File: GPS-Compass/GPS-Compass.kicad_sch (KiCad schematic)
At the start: 117 parts, among them IC1 TPS565242DRLR, J2 FFC2B28-12-G, J3 Motor_conn, J4 USB_TypeC, J5 FFC2B28-12-G, J7 01x10, M1 Stepper_Motor_bipolar, Q1 Q_PMOS, Q2 Q_PMOS, SW8 RESET, SW9 BOOT, U1 DRV8834RGER, U2 AP62300Z6, U3 USBLC6-2SC6, U4 ESP32-S3-WROOM-1, U5 BQ25887

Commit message: layout updates
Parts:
- BZ1: footprint gps-compass_brd:CEM-1203_Buzzer -> inset:AST0827MW-03BTRQ_MAL
- J2: renamed from J3; footprint (none) -> Connector_JST:JST_XH_B4B-XH-A_1x04_P2.50mm_Vertical
- renumbered C2 to C1, C13 to C10, C14 to C11, C15 to C12, C16 to C13, C17 to C14, C18 to C15, C19 to C16, C20 to C17, C21 to C18, C22 to C19, C3 to C2, C23 to C20, C24 to C21, C25 to C22, C26 to C23, C27 to C24, C28 to C25, C29 to C26, C5 to C3, C6 to C4, C7 to C5, C8 to C6, C10 to C7, C11 to C8, C12 to C9, J2 to J1, J5 to J3, J7 to J4, J4 to J5, R18 to R10, R19 to R11, R20 to R12, R21 to R13, R22 to R14, R23 to R15, R24 to R16, R25 to R17, R26 to R18, R27 to R19, R28 to R20, R29 to R21, R30 to R22, R31 to R23, R32 to R24, R33 to R25, R34 to R26, R35 to R27, R36 to R28, R37 to R29, R6 to R3, R38 to R30, R39 to R31, R40 to R32, R41 to R33, R42 to R34, R43 to R35, R44 to R36, R45 to R37, R7 to R4, R9 to R5, R12 to R6, R13 to R7, R14 to R8, R15 to R9, SW8 to SW1, SW9 to SW2
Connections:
- net DN_IN: no longer J5.A6 (DP1)
- net DP_IN: now also J5.A6 (DP1)
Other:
- moved on the sheet: J1, J3, M1

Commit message: layout updates
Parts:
- SW1: footprint Connector_Wire:SolderWire-0.1sqmm_1x02_P3.6mm_D0.4mm_OD1mm_Relief -> gps-compass_brd:SW_SPST_EVQPE1
- SW2: footprint Button_Switch_SMD:SW_SPST_B3U-1000P -> gps-compass_brd:SW_SPST_EVQPE1
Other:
- moved on the sheet: SW1

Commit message: routing
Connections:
- net +3V3: now also J3.11; no longer J3.2
- net +5V: now also J1.1, J1.2, J1.3; no longer J1.10, J1.11, J1.12
- net +8V: now also J3.3; no longer J3.10
- net CLK: now also J1.6; no longer J1.7
- net CRD_RST: now also J3.6; no longer J3.7
- net EN: now also J3.4; no longer J3.9
- net EXT0: now also J3.10; no longer J3.3
- net EXT1: now also J3.8; no longer J3.5
- net EXT2: now also J3.5; no longer J3.8
- net GND: now also J1.5, J1.7, J1.9, J3.9; no longer J1.4, J1.6, J1.8, J3.4
- net GNSS_RST: now also J3.2; no longer J3.11
- net LED_EXT0: now also J3.7; no longer J3.6
- net LED_EXT1: now also J3.12; no longer J3.1
- net MOSI: now also J1.4; no longer J1.9
- net MSW_ON: now also J3.1; no longer J3.12
- net ~{CS}: now also J1.8; no longer J1.5

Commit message: will be remaking the charger probably
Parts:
- removed JP5: Jumper, Jumper:SolderJumper-2_P1.3mm_Open_RoundedPad1.0x1.5mm, symbol Jumper:Jumper_2_Small_Open
- J2: footprint Connector_JST:JST_XH_B4B-XH-A_1x04_P2.50mm_Vertical -> Connector_JST:JST_XH_S4B-XH-SM4-TB_1x04-1MP_P2.50mm_Horizontal
- R36: value 0R -> 220R
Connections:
- net USB_VBUS: now also Q2.1 (G), R18.1
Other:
- note added: "1. FUEL GAUGE 2. LiPo/Li-Ion 3. 4. 5. 6. 7."
- note added: "https://cz.mouser.com/ProductDetail/Texas-Instruments/BQ25895MRTWR?qs=uNh9J9Y3wTe%2F%252BmcQbu7CLA%3D%3D"
- note removed: "1. BUTTONS? 2. FINISH SCHEMATIC 3. BOARD LAYOUT 4. 5. CONNECTORS 6. 7."
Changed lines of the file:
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@@
 	(rectangle
 		(start 300.99 163.195)
-		(end 427.355 281.305)
+		(end 427.355 281.94)
 		(stroke
 			(width 1)
@@
 		)
 	)
-	(text "1. BUTTONS?\n2. FINISH SCHEMATIC\n3. BOARD LAYOUT\n4. \n5. CONNECTORS\n6. \n7."
+	(text "1. FUEL GAUGE\n2. LiPo/Li-Ion\n3. \n4. \n5. \n6. \n7."
 		(exclude_from_sim no)
 		(at 19.685 307.975 0)
@@
 		)
 	)
+	(text "https://cz.mouser.com/ProductDetail/Texas-Instruments/BQ25895MRTWR?qs=uNh9J9Y3wTe%2F%252BmcQbu7CLA%3D%3D"
+		(exclude_from_sim no)
+		(at 361.95 144.145 0)
+		(effects
+			(font
+				(size 1.27 1.27)
+			)
+		)
+	)
 	(text "probs not meant to be connected to the MCU"
 		(exclude_from_sim no)
@@
 	(wire
 		(pts
-			(xy 323.85 59.69) (xy 325.12 59.69)
-		)
-		(stroke
-			(width 0)
-			(type default)
-		)
-	)
-	(wire
-		(pts
 			(xy 355.6 101.6) (xy 358.14 101.6)
 		)
@@
 	(wire
 		(pts
-			(xy 313.69 59.69) (xy 318.77 59.69)
+			(xy 318.77 59.69) (xy 325.12 59.69)
 		)
 		(stroke
@@
 	(wire
 		(pts
-			(xy 313.69 59.69) (xy 313.69 58.42)
+			(xy 318.77 59.69) (xy 318.77 58.42)
 		)
 		(stroke
@@
 	)
 	(image
-		(at -70.104 42.926)
+		(at -61.849 206.121)
 		(scale 0.414908)
 		(data "iVBORw0KGgoAAAANSUhEUgAAAh4AAAH+CAIAAABcDZACAAAAA3NCSVQICAjb4U/gAAAACXBIWXMA"
@@
 	)
 	(image
-		(at -72.771 111.76)
+		(at 494.919 116.84)
 		(scale 0.27793)
 		(data "iVBORw0KGgoAAAANSUhEUgAAAsgAAAJLCAIAAAB17fdXAAAAA3NCSVQICAjb4U/gAAAACXBIWXMA"
@@
 	)
 	(symbol
-		(lib_id "Jumper:Jumper_2_Small_Open")
-		(at 321.31 59.69 0)
-		(unit 1)
-		(exclude_from_sim no)
-		(in_bom no)
-		(on_board yes)
-		(dnp no)
-		(property "Reference" "JP5"
-			(at 321.31 55.245 0)
-			(effects
-				(font
-					(size 1 1)
-				)
-			)
-		)
-		(property "Value" "Jumper"
-			(at 321.31 57.15 0)
-			(effects
-				(font
-					(size 1 1)
-				)
-			)
-		)
-		(property "Footprint" "Jumper:SolderJumper-2_P1.3mm_Open_RoundedPad1.0x1.5mm"
-			(at 321.31 59.69 0)
-			(effects
-				(font
-					(size 1.27 1.27)
-				)
-				(hide yes)
-			)
-		)
-		(property "Datasheet" "~"
-			(at 321.31 59.69 0)
-			(effects
-				(font
-					(size 1.27 1.27)
-				)
-				(hide yes)
-			)
-		)
-		(property "Description" "Jumper, 2-pole, small symbol, open"
-			(at 321.31 59.69 0)
-			(effects
-				(font
-					(size 1.27 1.27)
-				)
-				(hide yes)
-			)
-		)
-		(pin "1"
-		)
-		(pin "2"
-		)
-		(instances
-			(project "GPS-Compass"
-				(path "/944f168e-b689-4be9-b5f1-4ef8c625b176"
-					(reference "JP5")
-					(unit 1)
-				)
-			)
-		)
-	)
-	(symbol
 		(lib_id "power:+3V3")
 		(at 55.88 198.12 90)
@@
 			)
 		)
-		(property "Footprint" "Connector_JST:JST_XH_B4B-XH-A_1x04_P2.50mm_Vertical"
+		(property "Footprint" "Connector_JST:JST_XH_S4B-XH-SM4-TB_1x04-1MP_P2.50mm_Horizontal"
 			(at 115.57 195.58 0)
 			(effects
@@
 	(symbol
 		(lib_id "power:+5V")
-		(at 313.69 58.42 0)
+		(at 318.77 58.42 0)
 		(unit 1)
 		(exclude_from_sim no)
@@
 		(dnp no)
 		(property "Reference" "#PWR066"
-			(at 313.69 62.23 0)
+			(at 318.77 62.23 0)
 			(effects
 				(font
@@
 		)
 		(property "Value" "USB_VBUS"
-			(at 313.69 54.61 0)
+			(at 318.77 54.61 0)
 			(effects
 				(font
@@
 		)
 		(property "Footprint" ""
-			(at 313.69 58.42 0)
+			(at 318.77 58.42 0)
 			(effects
 				(font
@@
 		)
 		(property "Datasheet" ""
-			(at 313.69 58.42 0)
+			(at 318.77 58.42 0)
 			(effects
 				(font
@@
 		)
 		(property "Description" "Power symbol creates a global label with name \"+5V\""
-			(at 313.69 58.42 0)
+			(at 318.77 58.42 0)
 			(effects
 				(font
@@
 			)
 		)
-		(property "Value" "0R"
+		(property "Value" "220R"
 			(at 400.685 227.33 0)
 			(effects

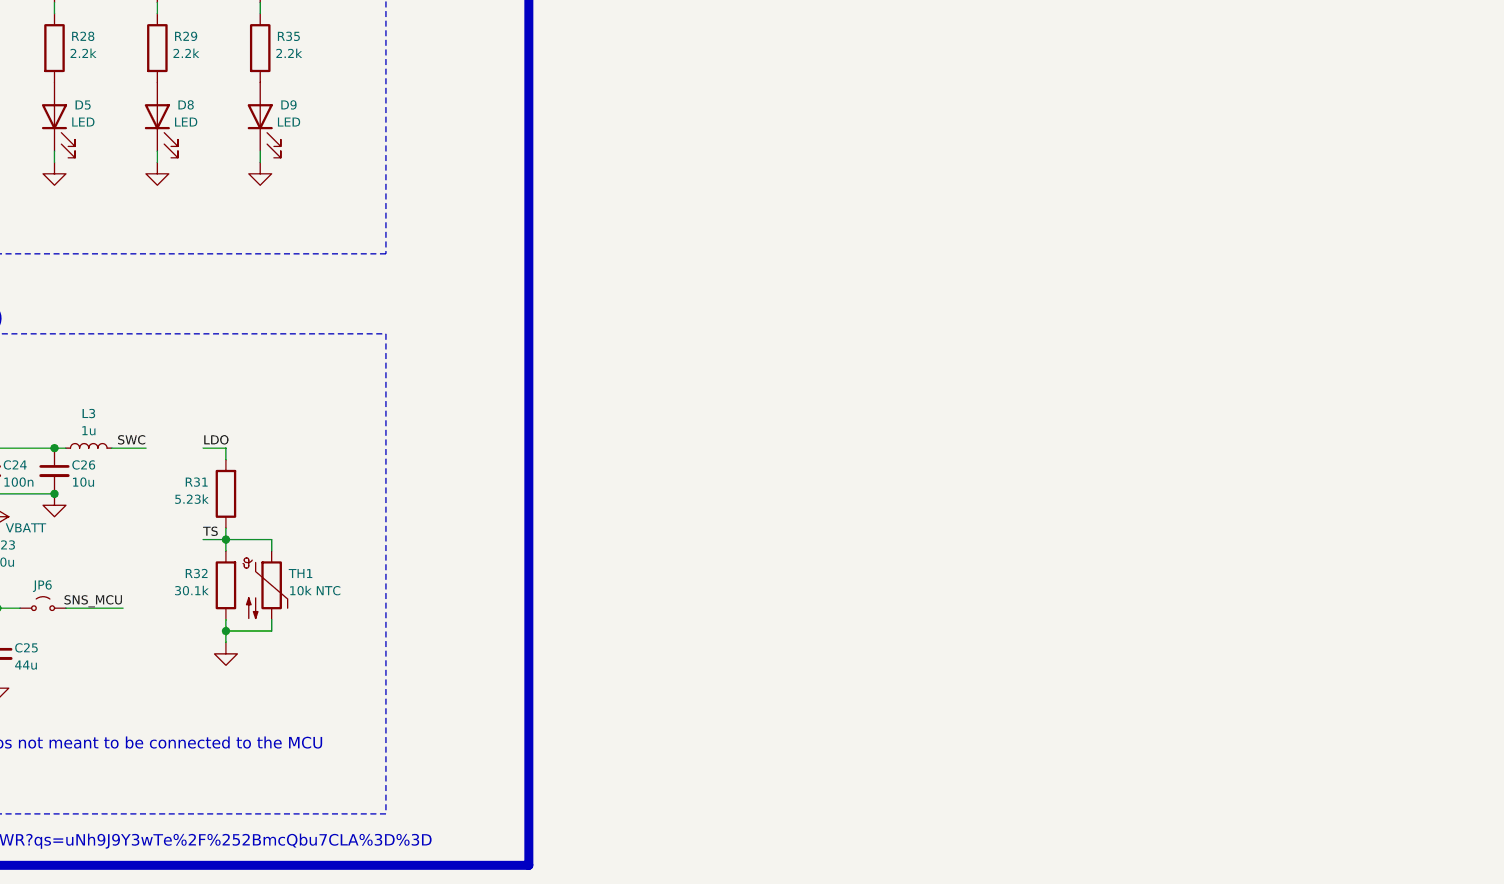
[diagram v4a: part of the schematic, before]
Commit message: new IC charger
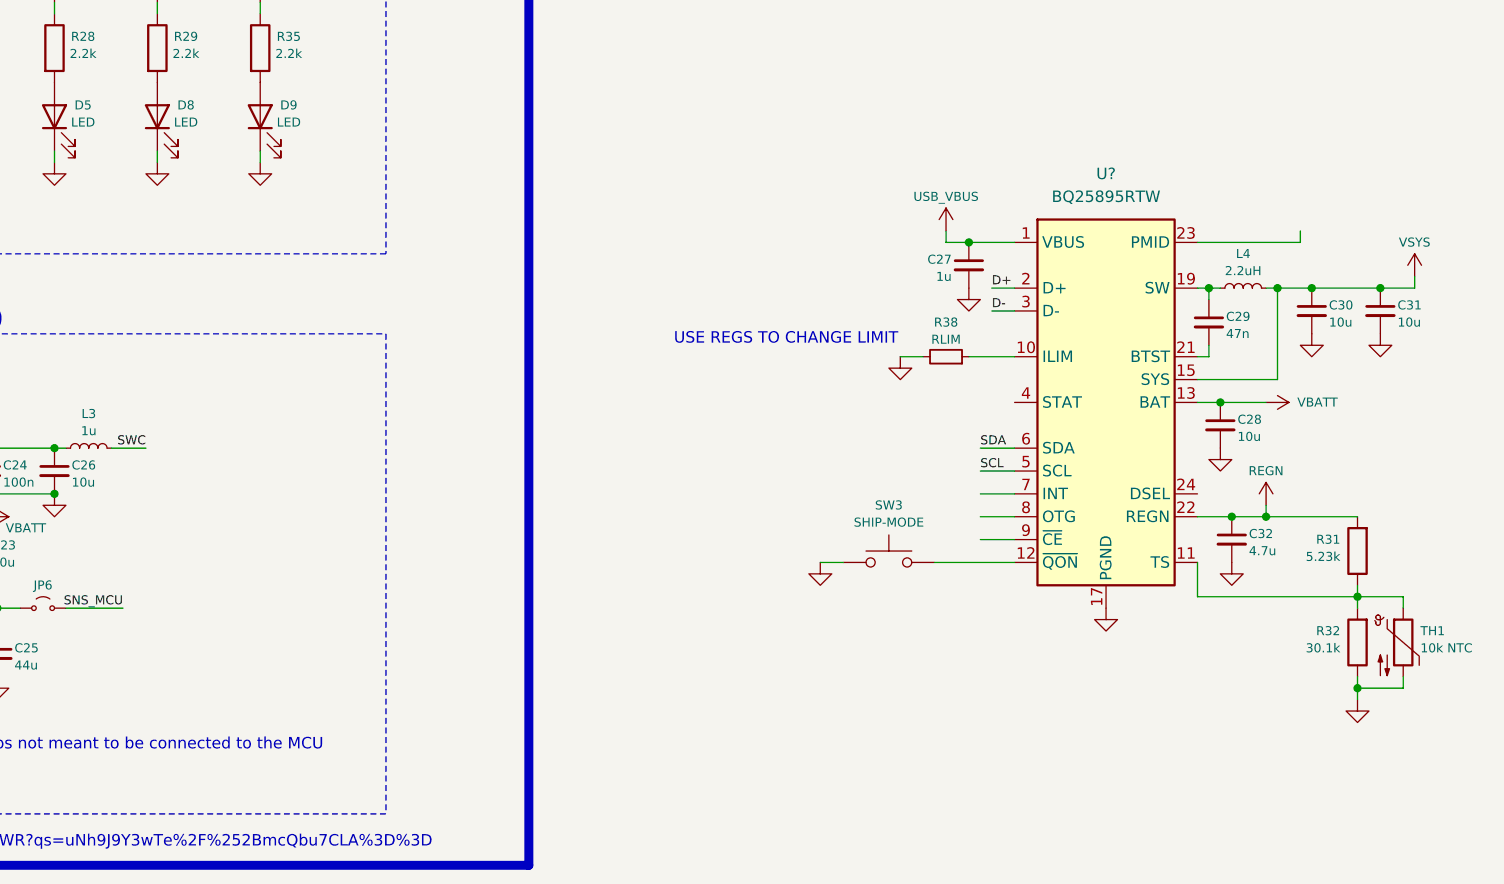
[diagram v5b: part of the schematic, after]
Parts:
- added C27: 1u, Capacitor_SMD:C_0805_2012Metric, symbol Device:C_Small
- added C28, C30, C31: 10u, Capacitor_SMD:C_0805_2012Metric, symbol Device:C_Small
- added C29: 47n, Capacitor_SMD:C_0805_2012Metric, symbol Device:C_Small
- added C32: 4.7u, Capacitor_SMD:C_0805_2012Metric, symbol Device:C_Small
- added L4: 2.2uH, Inductor_SMD:L_Walsin_WLFM201609x, symbol Device:L_Small
- added R38: RLIM, Resistor_SMD:R_0805_2012Metric, symbol Device:R_Small
- added SW3: SHIP-MODE, gps-compass_brd:SW_SPST_EVQPE1, symbol Switch:SW_Push
- added U?: BQ25895RTW, Package_DFN_QFN:Texas_RTW_WQFN-24-1EP_4x4mm_P0.5mm_EP2.7x2.7mm_ThermalVias, symbol Battery_Management:BQ25895RTW
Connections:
- net D+: now also U?.2 (D+)
- net D-: now also U?.3 (D-)
- net GND: now also C27.2, C28.2, C30.2, C31.2, C32.2, R38.2, SW3.1, U?.17 (PGND), U?.18 (PGND), U?.25 (PGND)
- net LDO: no longer R31.2
- net SCL: now also U?.5 (SCL)
- net SDA: now also U?.6 (SDA)
- net TS: no longer R31.1, R32.2, TH1.1
- net USB_VBUS: now also C27.1, U?.1 (VBUS)
- net VBATT: now also C28.1, U?.13 (BAT), U?.14 (BAT)
- new net: R31.1, R32.2, TH1.1, U?.11 (TS)
- new net: SW3.2, U?.12 (~{QON})
- new net: C29.1, L4.1, U?.19 (SW), U?.20 (SW)
- new net: C29.2, U?.21 (BTST)
- new net: R38.1, U?.10 (ILIM)
- new net REGN: C32.1, R31.2, U?.22 (REGN)
- new net VSYS: C30.1, C31.1, L4.2, U?.15 (SYS), U?.16 (SYS)
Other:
- note added: "USE REGS TO CHANGE LIMIT"
- moved on the sheet: R31, R32, TH1

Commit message: new usb charger
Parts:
- removed BT1: 2xLi-Ion_cells, gps-compass_brd:18650_2S_Holder, symbol gps-compass_sch:2xLi-Ion_cells
- removed C2, C6: 100n, Capacitor_SMD:C_0805_2012Metric, symbol Device:C_Small
- removed C7, C8: 22u, Capacitor_SMD:C_0805_2012Metric, symbol Device:C_Small
- removed D10: LED, LED_SMD:LED_0805_2012Metric, symbol Device:LED
- removed D2, D3: D_Schottky, Diode_SMD:D_1206_3216Metric, symbol Device:D_Schottky
- removed JP1: Jumper, Jumper:SolderJumper-3_P1.3mm_Open_RoundedPad1.0x1.5mm_NumberLabels, symbol Jumper:SolderJumper_3_Open
- removed L1: 3.3u, Inductor_SMD:L_Vishay_IHLP-1616, symbol Device:L
- removed Q2: Q_PMOS, Package_TO_SOT_SMD:SOT-23-3, symbol Device:Q_PMOS_GSD
- removed R18, R27, R37: 10k, Resistor_SMD:R_0805_2012Metric, symbol Device:R
- removed R30: 2.2k, Resistor_SMD:R_0805_2012Metric, symbol Device:R
- removed R7: 10k, Resistor_SMD:R_0805_2012Metric, symbol Device:R_Small
- removed U2: AP62300Z6, Package_TO_SOT_SMD:SOT-563, symbol Regulator_Switching:AP62300Z6
- added BT1: LiPo cell, TestPoint:TestPoint_Pad_D2.0mm, symbol Device:Battery_Cell
- added C25: 47u, Capacitor_SMD:C_1210_3225Metric, symbol Device:C_Small
- added C34: 22u, Capacitor_SMD:C_0805_2012Metric, symbol Device:C_Small
- added C35: 100n, Capacitor_SMD:C_0805_2012Metric, symbol Device:C_Small
- added J6: USB_TypeC, sumec_brd:HRO_TYPE-C-31-M-12, symbol sumec_sch_lib:USB_TypeC
- added J7: Conn_01x02_Pin, Connector_JST:JST_PH_S2B-PH-K_1x02_P2.00mm_Horizontal, symbol Connector:Conn_01x02_Pin
- added L5: 2,2u, Inductor_SMD:L_Murata_DFE201610P, symbol Device:L
- added R21: 2.2k, Resistor_SMD:R_0805_2012Metric, symbol Device:R
- added R37: 10k, Resistor_SMD:R_0805_2012Metric, symbol Device:R_Small
- added U7: TPS613222ADBV, Package_TO_SOT_SMD:SOT-23-5, symbol Regulator_Switching:TPS613222ADBV
- C1: value 10u -> 100n
- R24: value 2.2k -> 10k
- R4, R6: value 52.3k -> 36k
- gave numbers to parts that had none: 1
- renumbered C27 to C20, C29 to C21, C28 to C22, C32 to C23, C30 to C24, C31 to C26, C20 to C27, C21 to C28, C22 to C29, C23 to C30, C24 to C31, C25 to C32, C26 to C33, D11 to D10, D12 to D11, JP6 to JP5, L4 to L3, L3 to L4, R21 to R19, R38 to R20, R25 to R22, R26 to R23, R28 to R25, R29 to R26, R31 to R27, R32 to R28, R33 to R29, R34 to R30, R35 to R31, R36 to R32, R19 to R33, R20 to R34, R22 to R35, R23 to R36, U5 to U6
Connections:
- net +3V3: now also R24.2, R4.2, R6.2, R21.1, R37.1; no longer R24.1
- net +5V: now also C34.1, C35.1, U7.4 (VOUT); no longer C13.1, C14.1, IC1.1 (VIN), IC1.5 (EN)
- net +8V: no longer C1.1, Q1.3 (D), R3.1
- net 5V_CONV: no longer R6.1
- net GND: now also R3.2, BT1.2 (-), C25.2, C34.2, C35.2, J6.A1_B12 (GND), J6.B1_A12 (GND), J7.1 (Pin_1), U7.2 (GND); no longer R4.2
- net STAT: now also U5.4 (STAT)
- net TS: now also R27.1, R28.2, TH1.1, U5.11 (TS)
- net VBATT: now also BT1.1 (+), J7.2 (Pin_2); no longer Q1.2 (S), R5.1
- net VSYS: now also Q1.2 (S), R5.1
- net ~{INT}: no longer D4.1 (K)
- net at D4.2 (A): now also R21.2; no longer R24.2
- net VOTG: now reaches U5.23 (PMID)
- net VOTG: now also C25.1, J6.A4_B9 (VBUS), J6.B4_A9 (VBUS)
- net DSEL: now reaches U5.24 (DSEL)
- net DSEL: now also D4.1 (K), R24.1
- net INT: now reaches U5.7 (INT)
- net INT: now also R37.2
- net OTG: now reaches U5.8 (OTG)
- net ~{CE}: now reaches U5.9 (~{CE})
- net at R4.1: now also J6.B5 (CC2); no longer R3.2
- new net: C1.1, J6.S1 (SHIELD), J6.S2 (SHIELD), J6.S3 (SHIELD), J6.S4 (SHIELD), R3.1
- new net: J6.A5 (CC1), R6.1
- new net: L5.2, U7.1 (SW)
- new net VIN: C13.1, C14.1, IC1.1 (VIN), IC1.5 (EN), L5.1, Q1.3 (D)
- no-connect marks 14 -> 20
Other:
- note added: "1. FUEL GAUGE 2. LiPo/Li-Ion 3. add test points for charger IC 4. 5. 6. 7."
- note added: "CONNECTOR LINK"
- note added: "STEP-DOWN CONVERTER 3.3V"
- note added: "STEP-UP CONVERTER 5V"
- note added: "TPS613222ADBV Step-up converter Input: 0.9-5.5V Output: 5V Current output: 1.8A Quiescent Current: 6.5 uA Switching freq.: 1.6MHz Inductor Inductance: 2.2uH Max. current: 2.1A"
- note added: "USB C OTG CHARGER"
- note removed: "1. FUEL GAUGE 2. LiPo/Li-Ion 3. 4. 5. 6. 7."
- note removed: "AP62301Z6-7 Step down converter Input: 4.2-18V Output: 5V Current output: 3A Switching freq.: 750kHz Inductor Inductance: 3.3uH Max. current: 2.7A"
- note removed: "Power switching between 5V VBUS - USB and 5V Buck converter - BATT"
- note removed: "STEPDOWN CONVERTER 3.3V"
- note removed: "STEPDOWN CONVERTER 5V"
- note removed: "SWITCHING SIMULATION - FALSTAD"
- note removed: "USB POWER SWITCH"
- note removed: "good input source"
- note removed: "status and report"
- moved on the sheet: C13, C14, C17, C18, C19, C20, C21, C22, C23, C24, C26, C27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

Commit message: UI changes
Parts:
- added D1: LED, symbol Device:LED_Small
- added J8: Conn_01x02_Pin, Connector_Wire:SolderWire-0.1sqmm_1x02_P3.6mm_D0.4mm_OD1mm_Relief, symbol Connector:Conn_01x02_Pin
- added R11, R14, R3: 10k, Resistor_SMD:R_0805_2012Metric, symbol Device:R_Small
- added R4: 2.2K, Resistor_SMD:R_0805_2012Metric, symbol Device:R_Small
- added SW3: SW_SPDT, symbol Switch:SW_SPDT
- renumbered C35 to C1, C11 to C10, C17 to C11, C18 to C13, C19 to C14, C1 to C17, C20 to C18, C21 to C19, C3 to C2, C22 to C20, C23 to C21, C24 to C22, C25 to C23, C26 to C24, C27 to C25, C28 to C26, C29 to C27, C30 to C28, C31 to C29, C4 to C3, C32 to C30, C33 to C31, C34 to C4, C9 to C6, C13 to C7, C10 to C8, C14 to C9, D11 to D10, D5 to D2, D8 to D3, D9 to D4, D1 to D5, D4 to D6, D6 to D7, D7 to D8, D10 to D9, J7 to J2, J2 to J3, J3 to J4, J4 to J5, J5 to J6, J6 to J7, JP2 to JP1, JP3 to JP2, JP4 to JP3, JP5 to JP4, L5 to L1, R12 to R10, R13 to R12, R14 to R13, R25 to R17, R26 to R18, R3 to R19, R31 to R20, R4 to R21, R17 to R22, R19 to R23, R6 to R24, R37 to R25, R20 to R26, R21 to R27, R22 to R28, R23 to R29, R24 to R30, R29 to R31, R30 to R32, R27 to R33, R28 to R34, R32 to R35, R33 to R36, R34 to R37, R35 to R38, R36 to R39, R8 to R6, R9 to R7, R10 to R8, R11 to R9, SW3 to SW4, U7 to U2
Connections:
- net ~{CE} is gone; now on net GND: U5.9 (~{CE})
- net +3V3: now also D1.2 (A), R11.2, R14.2, R3.2
- net +8V: no longer J4.3
- net CLK: now also U4.6 (IO6)
- net DIR: now also U4.4 (IO4)
- net GND: now also J8.1 (Pin_1), SW3.2 (B)
- net INT: now also U4.39 (IO1)
- net MOSI: now also U4.17 (IO9)
- net OTG: now also J4.3, SW3.1 (A)
- net SCL: now also U4.7 (IO7), R14.1
- net SDA: now also U4.12 (IO8), R11.1
- net STEP: now also U4.38 (IO2)
- net VBATT: now also J8.2 (Pin_2)
- net ~{CS}: now also U4.5 (IO5)
- net NFAULT: no longer names the net of U1.13 (NFAULT)
- net NFAULT: now also R3.1, R4.2
- new net: D1.1 (K), R4.1
- no-connect marks 20 -> 21
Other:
- note added: "BATT. INDICATOR"
- moved on the sheet: C17, C18, C19, C2, C20, C21, C22, C23, C24, C5, D2, D3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

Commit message: jkolsd
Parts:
- removed J4: FFC2B28-12-G, gps-compass_brd:GCT_FFC2B28-12-G, symbol gps-compass_sch:FFC2B28-12-G
- removed SW3: SW_SPDT, symbol Switch:SW_SPDT
- added M2: FAN, Connector:FanPinHeader_1x04_P2.54mm_Vertical, symbol Motor:Fan_4pin
- added Q2: SI2393DS, Package_TO_SOT_SMD:SOT-23-3, symbol Device:Q_PMOS_GSD
- added R40: 10k, Resistor_SMD:R_0805_2012Metric, symbol Device:R_Small
- D1: footprint (none) -> LED_SMD:LED_0805_2012Metric
- Q1: value Q_PMOS -> SI2393DS
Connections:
- net +5V: now also Q2.2 (S), R40.1
- net GND: now also M2.1 (-)
- new net: M2.2 (+), Q2.3 (D)
- new net FAN_PWM: M2.4 (PWM)
- new net ~{FAN_SW}: Q2.1 (G), R40.2
- no-connect marks 21 -> 20
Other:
- note removed: "UI CONN"
- moved on the sheet: D6, R27, R30
